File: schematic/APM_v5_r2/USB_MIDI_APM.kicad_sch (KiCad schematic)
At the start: 6 parts, among them J16 USB_A_FEMALE, J17 MIDI_DGB, U9 USBLC6-2SC6

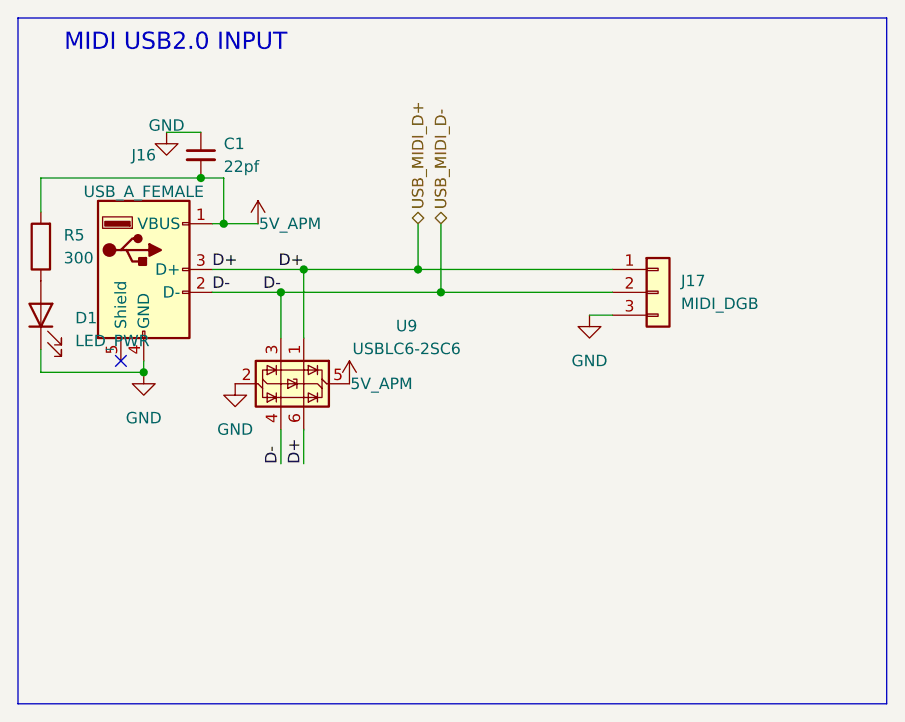
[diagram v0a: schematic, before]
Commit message: adding new rev of apm board with new routing and power management
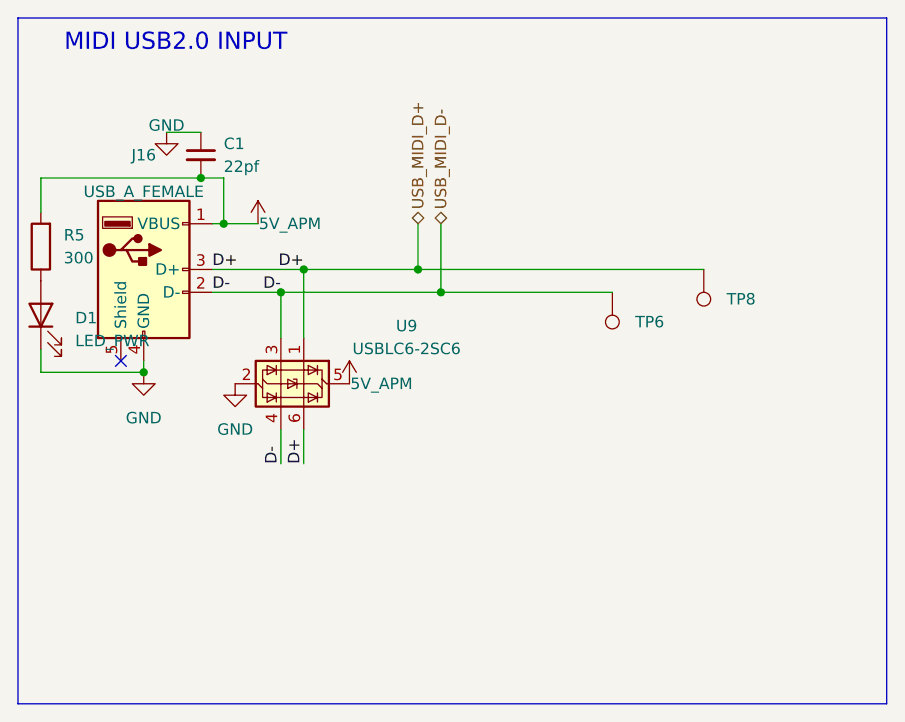
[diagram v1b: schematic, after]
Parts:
- removed J17: MIDI_DGB, Connector_PinHeader_2.54mm:PinHeader_1x03_P2.54mm_Vertical, symbol Connector_Generic:Conn_01x03
- added TP6: MIDI_D-, TestPoint:TestPoint_Pad_1.5x1.5mm, symbol Connector:TestPoint
- added TP8: MIDI_D+, TestPoint:TestPoint_Pad_1.5x1.5mm, symbol Connector:TestPoint
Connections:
- net USB_MIDI_D+: now also TP8.1
- net USB_MIDI_D-: now also TP6.1
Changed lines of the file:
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@@
-	(wire
-		(pts
-			(xy 152.4 96.52) (xy 154.94 96.52)
-		)
-		(stroke
-			(width 0)
-			(type default)
-		)
-	)
 	(wire
 		(pts
@@
 	(wire
 		(pts
-			(xy 133.35 91.44) (xy 154.94 91.44)
+			(xy 133.35 91.44) (xy 165.1 91.44)
 		)
 		(stroke
@@
 				(path "/63e257c1-2fa4-4533-ab9e-932d24befb8c/24833ad5-7cda-4ec3-a1f4-7117f67ff722"
 					(reference "J16")
-					(unit 1)
-				)
-			)
-		)
-	)
-	(symbol
-		(lib_id "power:GND")
-		(at 152.4 96.52 0)
-		(unit 1)
-		(body_style 1)
-		(exclude_from_sim no)
-		(in_bom yes)
-		(on_board yes)
-		(in_pos_files yes)
-		(dnp no)
-		(fields_autoplaced yes)
-		(property "Reference" "#PWR036"
-			(at 152.4 102.87 0)
-			(hide yes)
-			(show_name no)
-			(do_not_autoplace no)
-			(effects
-				(font
-					(size 1.27 1.27)
-				)
-			)
-		)
-		(property "Value" "GND"
-			(at 152.4 101.6 0)
-			(show_name no)
-			(do_not_autoplace no)
-			(effects
-				(font
-					(size 1.27 1.27)
-				)
-			)
-		)
-		(property "Footprint" ""
-			(at 152.4 96.52 0)
-			(hide yes)
-			(show_name no)
-			(do_not_autoplace no)
-			(effects
-				(font
-					(size 1.27 1.27)
-				)
-			)
-		)
-		(property "Datasheet" ""
-			(at 152.4 96.52 0)
-			(hide yes)
-			(show_name no)
-			(do_not_autoplace no)
-			(effects
-				(font
-					(size 1.27 1.27)
-				)
-			)
-		)
-		(property "Description" "Power symbol creates a global label with name \"GND\" , ground"
-			(at 152.4 96.52 0)
-			(hide yes)
-			(show_name no)
-			(do_not_autoplace no)
-			(effects
-				(font
-					(size 1.27 1.27)
-				)
-			)
-		)
-		(pin "1"
-		)
-		(instances
-			(project "APM"
-				(path "/63e257c1-2fa4-4533-ab9e-932d24befb8c/24833ad5-7cda-4ec3-a1f4-7117f67ff722"
-					(reference "#PWR036")
 					(unit 1)
 				)
@@
 	)
 	(symbol
+		(lib_id "Connector:TestPoint")
+		(at 154.94 93.98 180)
+		(unit 1)
+		(body_style 1)
+		(exclude_from_sim no)
+		(in_bom yes)
+		(on_board yes)
+		(in_pos_files yes)
+		(dnp no)
+		(fields_autoplaced yes)
+		(property "Reference" "TP6"
+			(at 157.48 97.2819 0)
+			(show_name no)
+			(do_not_autoplace no)
+			(effects
+				(font
+					(size 1.27 1.27)
+				)
+				(justify right)
+			)
+		)
+		(property "Value" "MIDI_D-"
+			(at 152.4 97.282 90)
+			(hide yes)
+			(show_name no)
+			(do_not_autoplace no)
+			(effects
+				(font
+					(size 1.27 1.27)
+				)
+			)
+		)
+		(property "Footprint" "TestPoint:TestPoint_Pad_1.5x1.5mm"
+			(at 149.86 93.98 0)
+			(hide yes)
+			(show_name no)
+			(do_not_autoplace no)
+			(effects
+				(font
+					(size 1.27 1.27)
+				)
+			)
+		)
+		(property "Datasheet" ""
+			(at 149.86 93.98 0)
+			(hide yes)
+			(show_name no)
+			(do_not_autoplace no)
+			(effects
+				(font
+					(size 1.27 1.27)
+				)
+			)
+		)
+		(property "Description" "test point"
+			(at 154.94 93.98 0)
+			(hide yes)
+			(show_name no)
+			(do_not_autoplace no)
+			(effects
+				(font
+					(size 1.27 1.27)
+				)
+			)
+		)
+		(pin "1"
+		)
+		(instances
+			(project "APM"
+				(path "/63e257c1-2fa4-4533-ab9e-932d24befb8c/24833ad5-7cda-4ec3-a1f4-7117f67ff722"
+					(reference "TP6")
+					(unit 1)
+				)
+			)
+		)
+	)
+	(symbol
 		(lib_id "power:GND")
 		(at 102.87 102.87 0)
@@
 				(path "/63e257c1-2fa4-4533-ab9e-932d24befb8c/24833ad5-7cda-4ec3-a1f4-7117f67ff722"
 					(reference "#PWR028")
-					(unit 1)
-				)
-			)
-		)
-	)
-	(symbol
-		(lib_id "Connector_Generic:Conn_01x03")
-		(at 160.02 93.98 0)
-		(unit 1)
-		(body_style 1)
-		(exclude_from_sim no)
-		(in_bom yes)
-		(on_board yes)
-		(in_pos_files yes)
-		(dnp no)
-		(fields_autoplaced yes)
-		(property "Reference" "J17"
-			(at 162.56 92.7099 0)
-			(show_name no)
-			(do_not_autoplace no)
-			(effects
-				(font
-					(size 1.27 1.27)
-				)
-				(justify left)
-			)
-		)
-		(property "Value" "MIDI_DGB"
-			(at 162.56 95.2499 0)
-			(show_name no)
-			(do_not_autoplace no)
-			(effects
-				(font
-					(size 1.27 1.27)
-				)
-				(justify left)
-			)
-		)
-		(property "Footprint" "Connector_PinHeader_2.54mm:PinHeader_1x03_P2.54mm_Vertical"
-			(at 160.02 93.98 0)
-			(hide yes)
-			(show_name no)
-			(do_not_autoplace no)
-			(effects
-				(font
-					(size 1.27 1.27)
-				)
-			)
-		)
-		(property "Datasheet" ""
-			(at 160.02 93.98 0)
-			(hide yes)
-			(show_name no)
-			(do_not_autoplace no)
-			(effects
-				(font
-					(size 1.27 1.27)
-				)
-			)
-		)
-		(property "Description" "Generic connector, single row, 01x03, script generated (kicad-library-utils/schlib/autogen/connector/)"
-			(at 160.02 93.98 0)
-			(hide yes)
-			(show_name no)
-			(do_not_autoplace no)
-			(effects
-				(font
-					(size 1.27 1.27)
-				)
-			)
-		)
-		(pin "2"
-		)
-		(pin "3"
-		)
-		(pin "1"
-		)
-		(instances
-			(project "APM"
-				(path "/63e257c1-2fa4-4533-ab9e-932d24befb8c/24833ad5-7cda-4ec3-a1f4-7117f67ff722"
-					(reference "J17")
 					(unit 1)
 				)
@@
 					(unit 1)
 				)
+			)
+		)
+	)
+	(symbol
+		(lib_id "Connector:TestPoint")
+		(at 165.1 91.44 180)
+		(unit 1)
+		(body_style 1)
+		(exclude_from_sim no)
+		(in_bom yes)
+		(on_board yes)
+		(in_pos_files yes)
+		(dnp no)
+		(fields_autoplaced yes)
+		(property "Reference" "TP8"
+			(at 167.64 94.7419 0)
+			(show_name no)
+			(do_not_autoplace no)
+			(effects
+				(font
+					(size 1.27 1.27)
+				)
+				(justify right)
+			)
+		)
+		(property "Value" "MIDI_D+"
+			(at 162.56 94.742 90)
+			(hide yes)
+			(show_name no)
+			(do_not_autoplace no)
+			(effects
+				(font
+					(size 1.27 1.27)
+				)
+			)
+		)
+		(property "Footprint" "TestPoint:TestPoint_Pad_1.5x1.5mm"
+			(at 160.02 91.44 0)
+			(hide yes)
+			(show_name no)
+			(do_not_autoplace no)
+			(effects
+				(font
+					(size 1.27 1.27)
+				)
+			)
+		)
+		(property "Datasheet" ""
+			(at 160.02 91.44 0)
+			(hide yes)
+			(show_name no)
+			(do_not_autoplace no)
+			(effects
+				(font
+					(size 1.27 1.27)
+				)
+			)
+		)
+		(property "Description" "test point"
+			(at 165.1 91.44 0)
+			(hide yes)
+			(show_name no)
+			(do_not_autoplace no)
+			(effects
+				(font
+					(size 1.27 1.27)
+				)
+			)
+		)
+		(pin "1"
+		)
+		(instances
+			(project "APM"
+				(path "/63e257c1-2fa4-4533-ab9e-932d24befb8c/24833ad5-7cda-4ec3-a1f4-7117f67ff722"
+					(reference "TP8")
+					(unit 1)
+				)

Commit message: renders. APM V5 R2 placement. going on with routing
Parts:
- TP6, TP8: footprint TestPoint:TestPoint_Pad_1.5x1.5mm -> TestPoint:TestPoint_Pad_D1.0mm
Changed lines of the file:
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@@
 		)
 		(instances
-			(project "APM"
+			(project "kicadrt_analysis_APM"
 				(path "/63e257c1-2fa4-4533-ab9e-932d24befb8c/24833ad5-7cda-4ec3-a1f4-7117f67ff722"
 					(reference "#PWR029")
@@
 		)
 		(instances
-			(project "APM"
+			(project "kicadrt_analysis_APM"
 				(path "/63e257c1-2fa4-4533-ab9e-932d24befb8c/24833ad5-7cda-4ec3-a1f4-7117f67ff722"
 					(reference "J16")
@@
 		)
 		(instances
-			(project "APM"
+			(project "kicadrt_analysis_APM"
 				(path "/63e257c1-2fa4-4533-ab9e-932d24befb8c/24833ad5-7cda-4ec3-a1f4-7117f67ff722"
 					(reference "D1")
@@
 			)
 		)
-		(property "Footprint" "TestPoint:TestPoint_Pad_1.5x1.5mm"
+		(property "Footprint" "TestPoint:TestPoint_Pad_D1.0mm"
 			(at 149.86 93.98 0)
 			(hide yes)
@@
 		)
 		(instances
-			(project "APM"
+			(project "kicadrt_analysis_APM"
 				(path "/63e257c1-2fa4-4533-ab9e-932d24befb8c/24833ad5-7cda-4ec3-a1f4-7117f67ff722"
 					(reference "TP6")
@@
 		)
 		(instances
-			(project "APM"
+			(project "kicadrt_analysis_APM"
 				(path "/63e257c1-2fa4-4533-ab9e-932d24befb8c/24833ad5-7cda-4ec3-a1f4-7117f67ff722"
 					(reference "#PWR028")
@@
 		)
 		(instances
-			(project "APM"
+			(project "kicadrt_analysis_APM"
 				(path "/63e257c1-2fa4-4533-ab9e-932d24befb8c/24833ad5-7cda-4ec3-a1f4-7117f67ff722"
 					(reference "#PWR032")
@@
 		)
 		(instances
-			(project "APM"
+			(project "kicadrt_analysis_APM"
 				(path "/63e257c1-2fa4-4533-ab9e-932d24befb8c/24833ad5-7cda-4ec3-a1f4-7117f67ff722"
 					(reference "#PWR031")
@@
 		)
 		(instances
-			(project "APM"
+			(project "kicadrt_analysis_APM"
 				(path "/63e257c1-2fa4-4533-ab9e-932d24befb8c/24833ad5-7cda-4ec3-a1f4-7117f67ff722"
 					(reference "U9")
@@
 			)
 		)
-		(property "Footprint" "TestPoint:TestPoint_Pad_1.5x1.5mm"
+		(property "Footprint" "TestPoint:TestPoint_Pad_D1.0mm"
 			(at 160.02 91.44 0)
 			(hide yes)
@@
 		)
 		(instances
-			(project "APM"
+			(project "kicadrt_analysis_APM"
 				(path "/63e257c1-2fa4-4533-ab9e-932d24befb8c/24833ad5-7cda-4ec3-a1f4-7117f67ff722"
 					(reference "TP8")
@@
 		)
 		(instances
-			(project "APM"
+			(project "kicadrt_analysis_APM"
 				(path "/63e257c1-2fa4-4533-ab9e-932d24befb8c/24833ad5-7cda-4ec3-a1f4-7117f67ff722"
 					(reference "R5")
@@
 		)
 		(instances
-			(project "APM"
+			(project "kicadrt_analysis_APM"
 				(path "/63e257c1-2fa4-4533-ab9e-932d24befb8c/24833ad5-7cda-4ec3-a1f4-7117f67ff722"
 					(reference "C1")
@@
 		)
 		(instances
-			(project "APM"
+			(project "kicadrt_analysis_APM"
 				(path "/63e257c1-2fa4-4533-ab9e-932d24befb8c/24833ad5-7cda-4ec3-a1f4-7117f67ff722"
 					(reference "#PWR030")
